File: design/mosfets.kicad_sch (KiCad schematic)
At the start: 33 parts, among them Q1 IRFS7530, Q2 IRFS7530, Q3 IRFS7530, Q4 IRFS7530, Q5 IRFS7530, Q6 IRFS7530, U4 INA826AIDR, U6 OPA333AIDBVR, U7 INA826AIDR, U9 OPA333AIDBVR

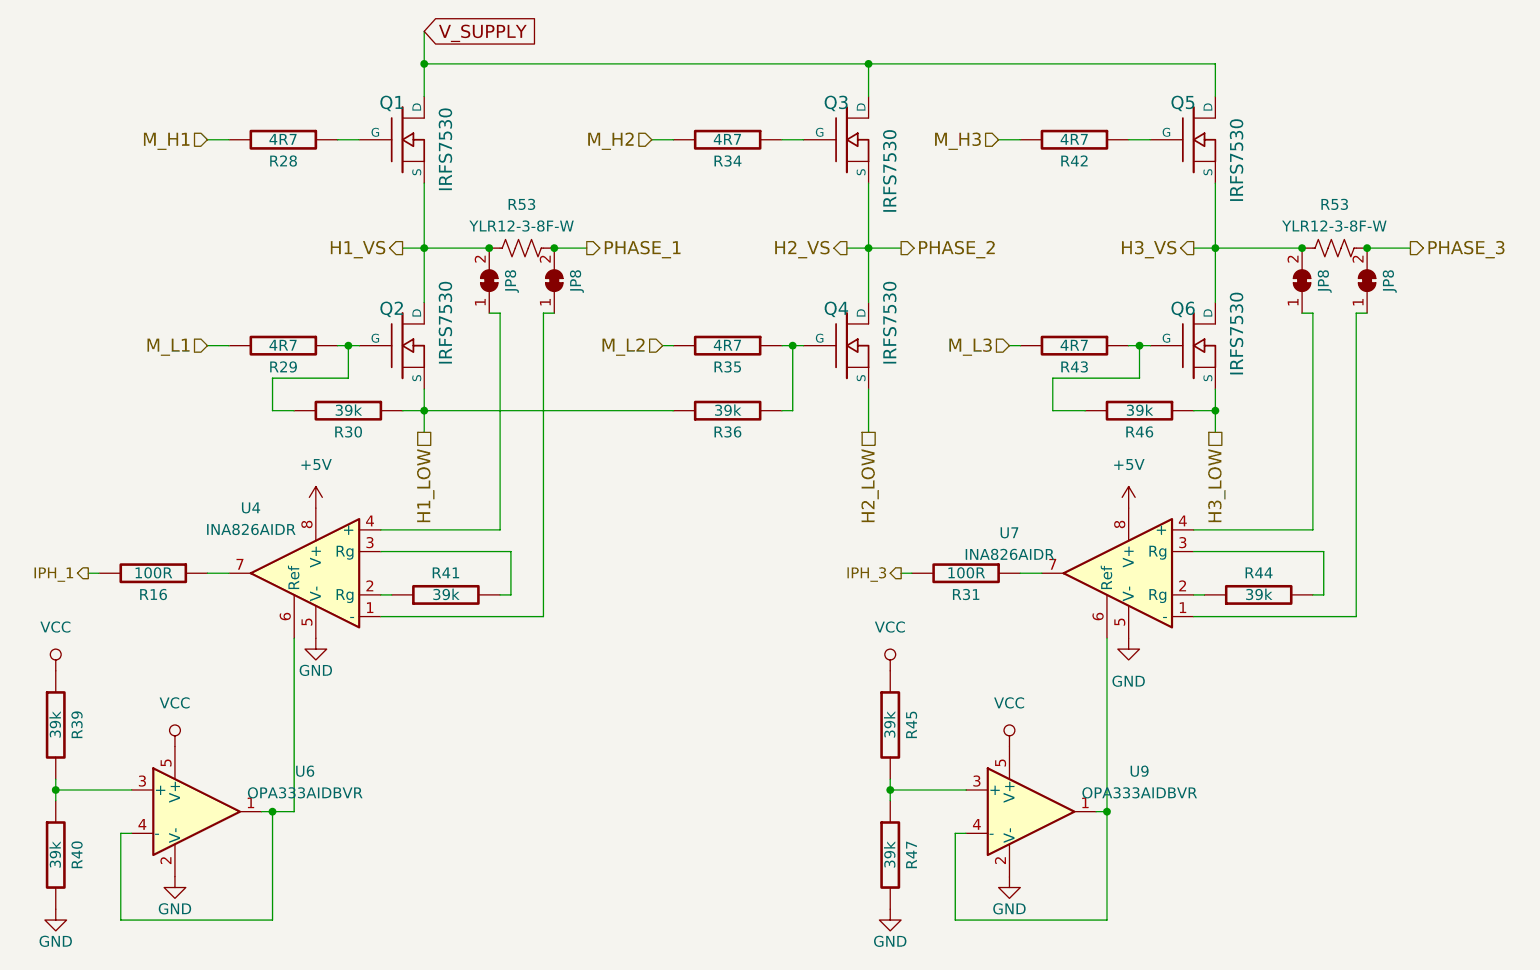
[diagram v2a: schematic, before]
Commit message: Fixing voltage supply of INA826 to read phase current value
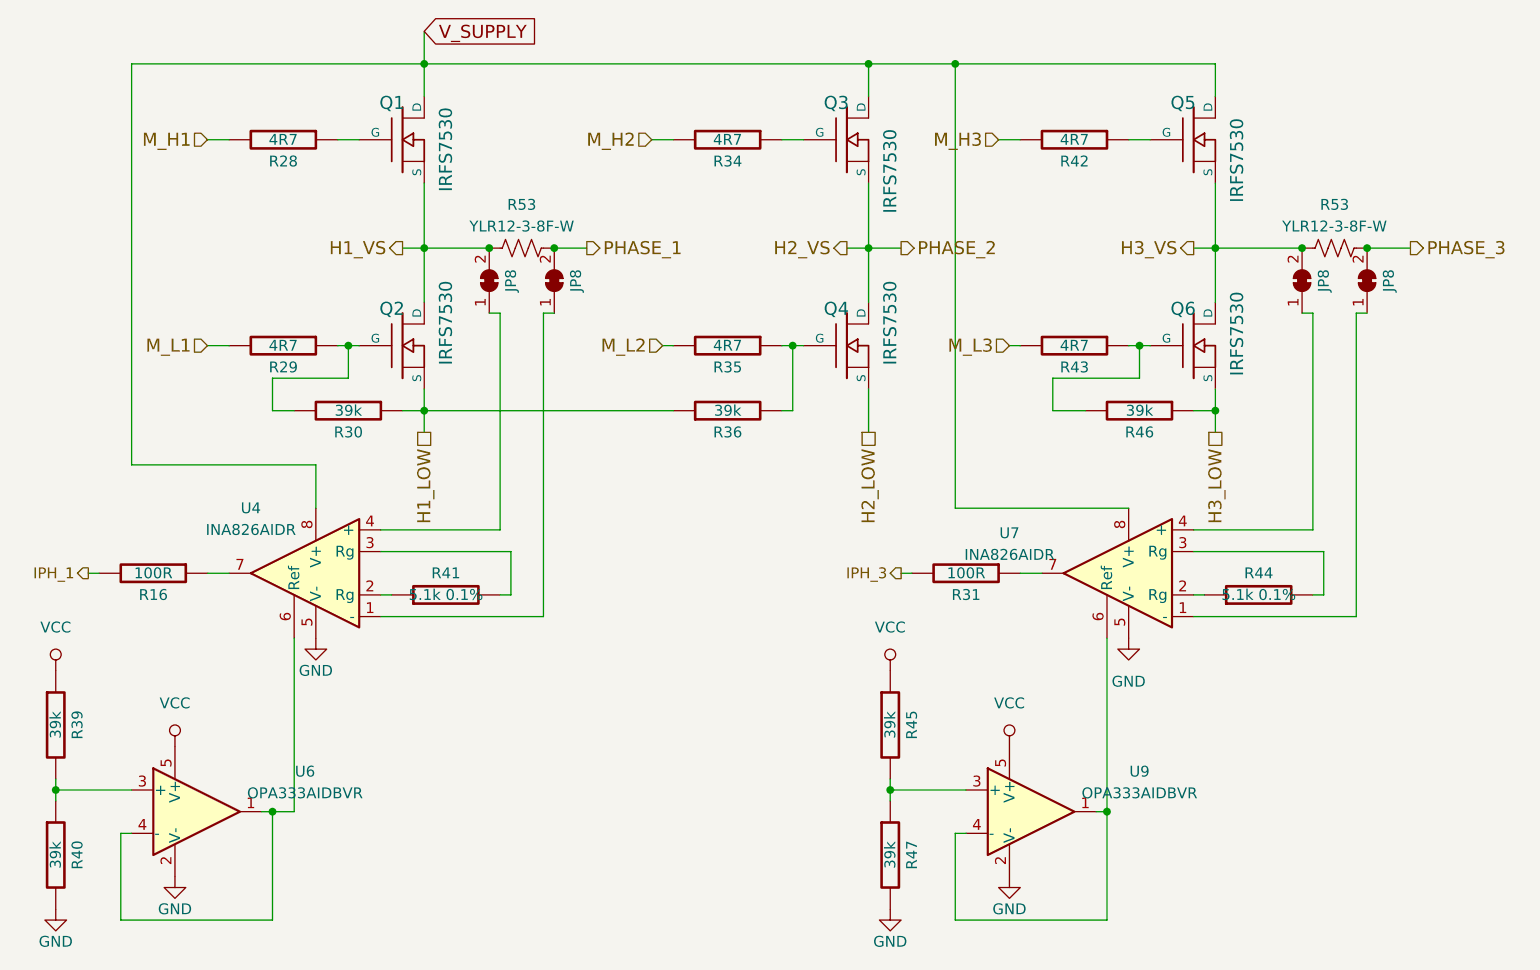
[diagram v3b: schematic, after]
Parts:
- R41, R44: value 39k -> 5.1k 0.1%
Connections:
- net +5V is gone; now on net V_SUPPLY: U4.8 (V+), U7.8 (V+)
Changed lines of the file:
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@@
   (junction (at 115.57 102.87) (diameter 0) (color 0 0 0 0)
   )
+  (junction (at 177.8 62.23) (diameter 0) (color 0 0 0 0)
+  )
   (junction (at 208.28 102.87) (diameter 0) (color 0 0 0 0)
   )
@@
     (stroke (width 0) (type default))
   )
+  (wire (pts (xy 81.28 62.23) (xy 115.57 62.23))
+    (stroke (width 0) (type default))
+  )
   (wire (pts (xy 170.18 147.32) (xy 170.18 148.59))
     (stroke (width 0) (type default))
@@
     (stroke (width 0) (type default))
   )
+  (wire (pts (xy 177.8 62.23) (xy 208.28 62.23))
+    (stroke (width 0) (type default))
+  )
   (wire (pts (xy 129.54 127) (xy 110.49 127))
     (stroke (width 0) (type default))
@@
     (stroke (width 0) (type default))
   )
+  (wire (pts (xy 177.8 62.23) (xy 177.8 114.3))
+    (stroke (width 0) (type default))
+  )
   (wire (pts (xy 185.42 121.92) (xy 187.96 121.92))
     (stroke (width 0) (type default))
@@
     (stroke (width 0) (type default))
   )
-  (wire (pts (xy 167.64 62.23) (xy 208.28 62.23))
+  (wire (pts (xy 167.64 62.23) (xy 177.8 62.23))
     (stroke (width 0) (type default))
   )
@@
     (stroke (width 0) (type default))
   )
+  (wire (pts (xy 81.28 109.22) (xy 81.28 62.23))
+    (stroke (width 0) (type default))
+  )
   (wire (pts (xy 97.79 99.06) (xy 97.79 102.87))
     (stroke (width 0) (type default))
@@
     (stroke (width 0) (type default))
   )
+  (wire (pts (xy 102.87 114.3) (xy 102.87 109.22))
+    (stroke (width 0) (type default))
+  )
   (wire (pts (xy 189.23 102.87) (xy 193.04 102.87))
     (stroke (width 0) (type default))
@@
     (stroke (width 0) (type default))
   )
+  (wire (pts (xy 198.12 114.3) (xy 177.8 114.3))
+    (stroke (width 0) (type default))
+  )
   (wire (pts (xy 208.28 62.23) (xy 208.28 66.04))
     (stroke (width 0) (type default))
@@
   )
   (wire (pts (xy 115.57 83.82) (xy 123.19 83.82))
+    (stroke (width 0) (type default))
+  )
+  (wire (pts (xy 102.87 109.22) (xy 81.28 109.22))
     (stroke (width 0) (type default))
   )
@@
       (effects (font (size 1.27 1.27)))
     )
-    (property "Value" "39k" (at 213.36 124.46 90)
+    (property "Value" "5.1k 0.1%" (at 213.36 124.46 90)
       (effects (font (size 1.27 1.27)))
     )
@@
       (effects (font (size 1.27 1.27)))
     )
-    (property "Value" "39k" (at 118.11 124.46 90)
+    (property "Value" "5.1k 0.1%" (at 118.11 124.46 90)
       (effects (font (size 1.27 1.27)))
     )
@@
         (path "/f0823096-6b01-491e-b593-a00aa44575f0/00000000-0000-0000-0000-000053f826dc"
           (reference "R14") (unit 1)
-        )
-      )
-    )
-  )
-  (symbol (lib_id "BLDC_4-rescue:+5V") (at 198.12 114.3 0) (unit 1)
-    (in_bom yes) (on_board yes) (dnp no) (fields_autoplaced)
-    (property "Reference" "#PWR079" (at 198.12 118.11 0)
-      (effects (font (size 1.27 1.27)) hide)
-    )
-    (property "Value" "+5V" (at 198.12 109.22 0)
-      (effects (font (size 1.27 1.27)))
-    )
-    (property "Footprint" "" (at 198.12 114.3 0)
-      (effects (font (size 1.524 1.524)))
-    )
-    (property "Datasheet" "" (at 198.12 114.3 0)
-      (effects (font (size 1.524 1.524)))
-    )
-    (pin "1")
-    (instances
-      (project "BLDC_4"
-        (path "/f0823096-6b01-491e-b593-a00aa44575f0/00000000-0000-0000-0000-000053f826dc"
-          (reference "#PWR079") (unit 1)
         )
       )
@@
         )
       )
-    )
-  )
-  (symbol (lib_id "BLDC_4-rescue:+5V") (at 102.87 114.3 0) (unit 1)
-    (in_bom yes) (on_board yes) (dnp no) (fields_autoplaced)
-    (property "Reference" "#PWR077" (at 102.87 118.11 0)
-      (effects (font (size 1.27 1.27)) hide)
-    )
-    (property "Value" "+5V" (at 102.87 109.22 0)
-      (effects (font (size 1.27 1.27)))
-    )
-    (property "Footprint" "" (at 102.87 114.3 0)
-      (effects (font (size 1.524 1.524)))
-    )
-    (property "Datasheet" "" (at 102.87 114.3 0)
-      (effects (font (size 1.524 1.524)))
-    )
-    (pin "1")
-    (instances
-      (project "BLDC_4"
-        (path "/f0823096-6b01-491e-b593-a00aa44575f0/00000000-0000-0000-0000-000053f826dc"
-          (reference "#PWR077") (unit 1)
-        )
-      )
